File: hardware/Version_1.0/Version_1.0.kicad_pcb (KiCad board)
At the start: 4 copper layers, 30 x 49 mm, 61 parts, among them J1 Conn_02x05_Counter_Clockwise, J2 Conn_Coaxial, J3 Conn_Coaxial, J4 Conn_Coaxial, J5 Conn_Coaxial, J6 Conn_Coaxial, U1 ADF4351, Y1 SG-5032CAN

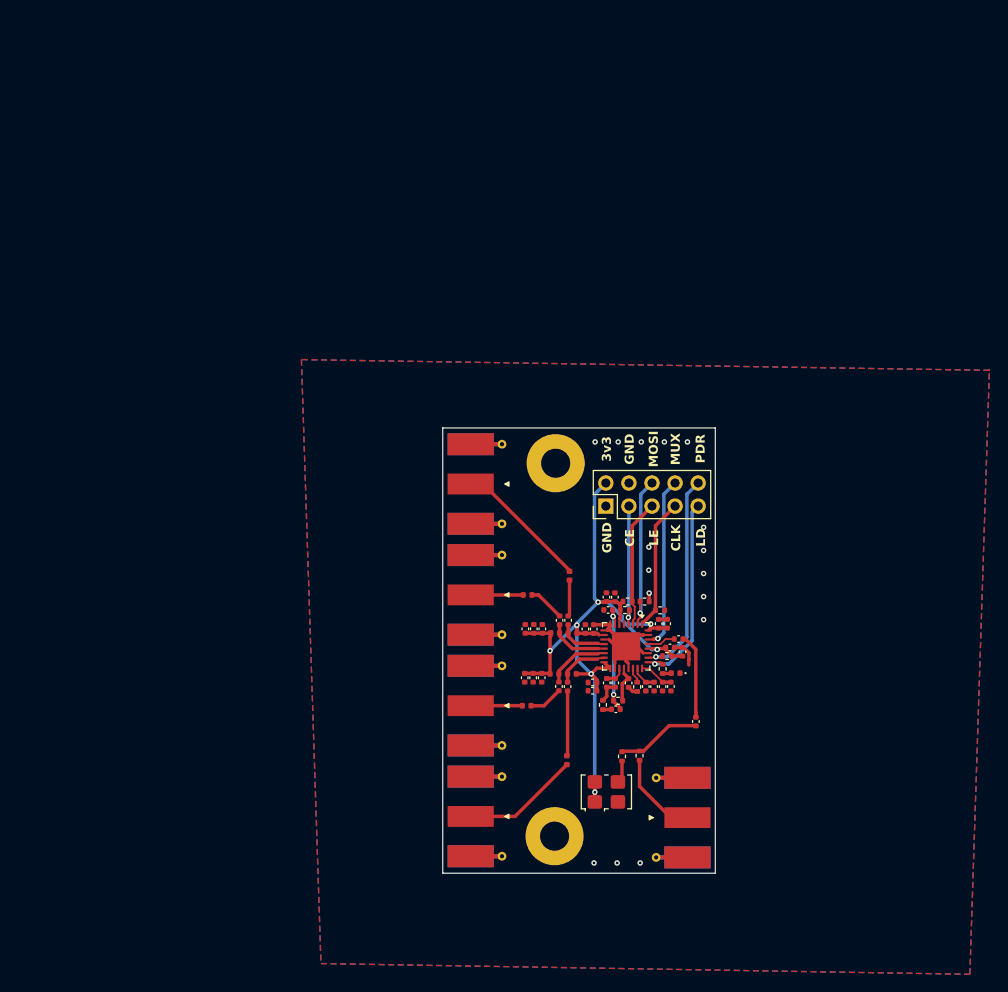
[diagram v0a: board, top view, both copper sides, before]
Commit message: completed version 2 and version 3 pcb and production files completed
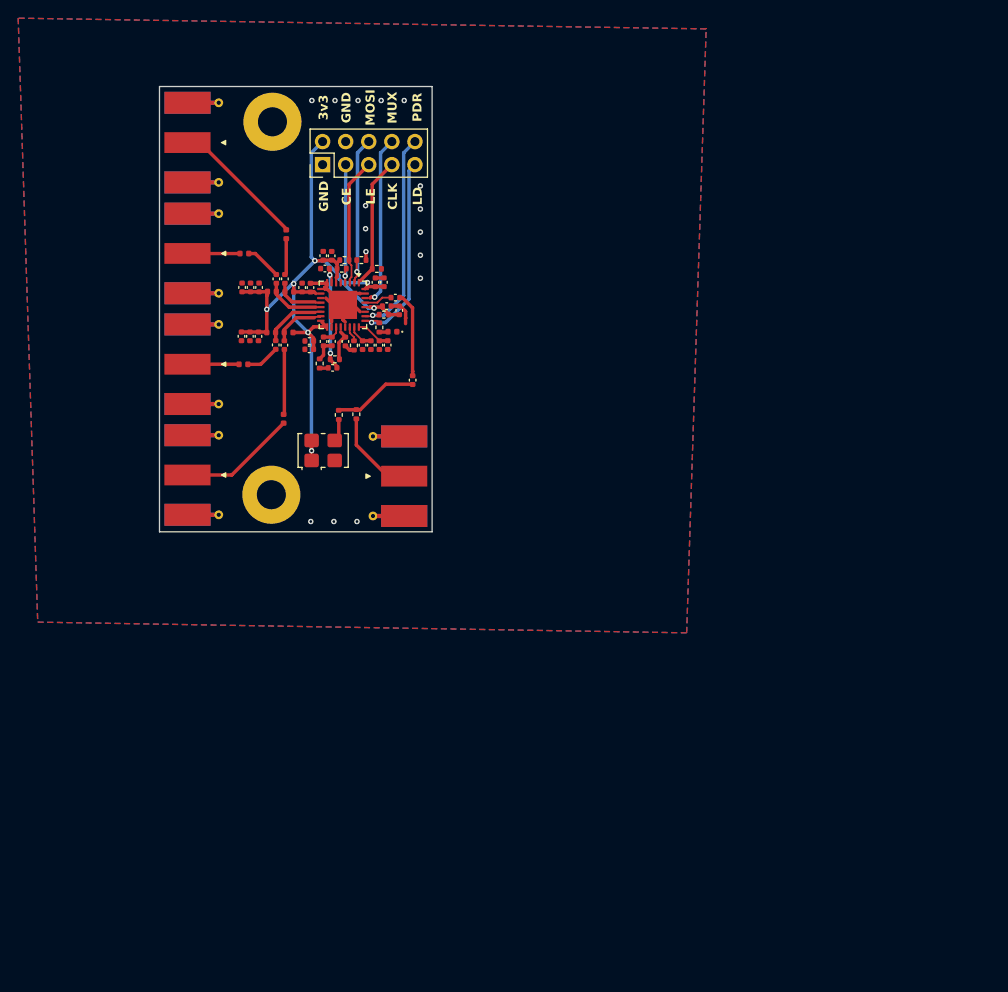
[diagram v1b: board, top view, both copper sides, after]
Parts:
- moved C25 48.8 mm to (102.2, 63.9)
- moved J2 48.8 mm to (102.3, 78.3)
- moved C1 48.8 mm to (93.6, 63.4)
- moved C11 48.8 mm to (90.9, 56.6)
- moved C12 48.8 mm to (88.1, 57.5)
- moved C13 48.8 mm to (87.1, 57.5)
- moved C14 48.8 mm to (86.2, 57.5)
- moved C15 48.8 mm to (90.0, 56.6)
- moved C17 48.8 mm to (103.1, 58.7)
- moved C19 48.8 mm to (86.1, 62.9)
- moved C21 48.8 mm to (96.1, 63.5)
- moved C22 48.8 mm to (99.5, 63.9)
- moved C26 48.8 mm to (95.3, 55.5)
- moved C28 48.8 mm to (97.6, 63.5)
- moved C29 48.8 mm to (87.1, 62.9)
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
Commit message: updates
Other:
- board text added: "OUTA+"
- board text added: "OUTA-"
- board text added: "OUTB+"
- board text added: "OUTB-"
- board text added: "REFIN"
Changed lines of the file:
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@@
 		(layer "Edge.Cuts")
+	)
+	(gr_text "OUTB-"
+		(at 85.27 76.64 0)
+		(layer "F.SilkS")
+		(effects
+			(font
+				(size 1 1)
+				(thickness 0.25)
+				(bold yes)
+			)
+			(justify bottom)
+		)
+	)
+	(gr_text "OUTA-"
+		(at 85.33 52.26 0)
+		(layer "F.SilkS")
+		(effects
+			(font
+				(size 1 1)
+				(thickness 0.25)
+				(bold yes)
+			)
+			(justify bottom)
+		)
+	)
+	(gr_text "OUTB+"
+		(at 85.33 68.74 0)
+		(layer "F.SilkS")
+		(effects
+			(font
+				(size 1 1)
+				(thickness 0.25)
+				(bold yes)
+			)
+			(justify bottom)
+		)
+	)
+	(gr_text "OUTA+"
+		(at 85.39 44.47 0)
+		(layer "F.SilkS")
+		(effects
+			(font
+				(size 1 1)
+				(thickness 0.25)
+				(bold yes)
+			)
+			(justify bottom)
+		)
+	)
+	(gr_text "REFIN"
+		(at 99.34 81.07 0)
+		(layer "F.SilkS")
+		(effects
+			(font
+				(size 1 1)
+				(thickness 0.25)
+				(bold yes)
+			)
+			(justify bottom)
+		)
 	)
 	(gr_text "3v3"
